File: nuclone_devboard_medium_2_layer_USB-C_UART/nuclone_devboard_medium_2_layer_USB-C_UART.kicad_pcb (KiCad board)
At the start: 2 copper layers, 50 x 76.2 mm, 36 parts, among them J1 JTAG_2X05, J2 TYPE-C-31-M-12, J5 Conn_02x06_Odd_Even, SW1 RESET, SW2 Bootloader, U1 MCP1702-3.3V, U2 TPESD0504C6

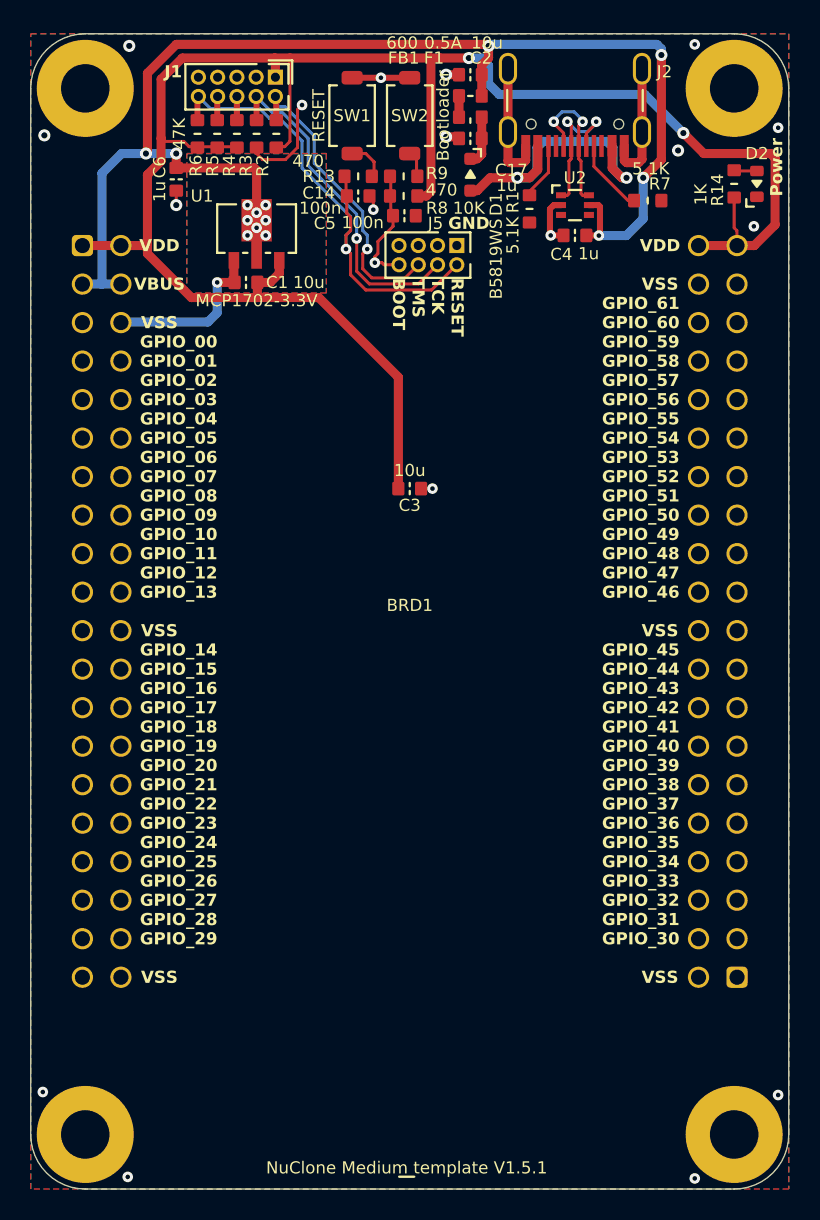
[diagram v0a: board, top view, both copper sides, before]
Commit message: updated medium nuclone footprint in templates, updated library
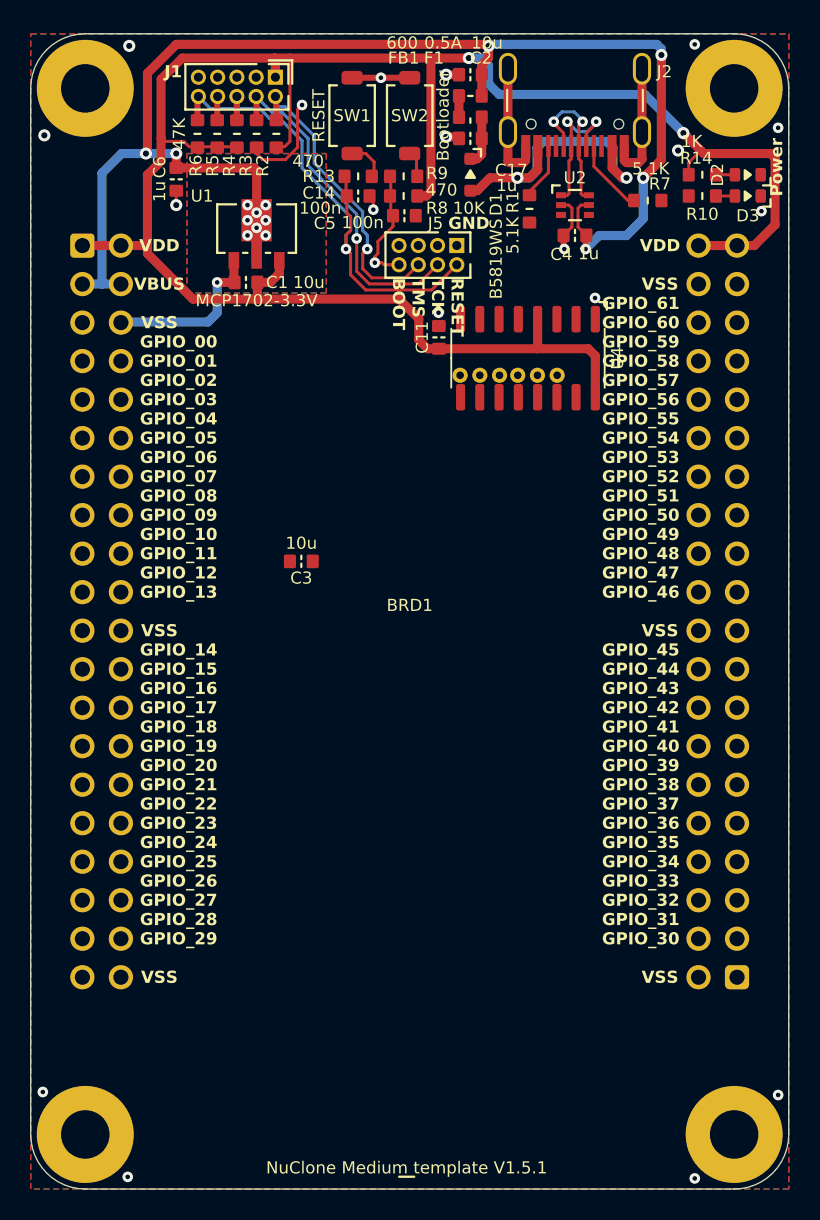
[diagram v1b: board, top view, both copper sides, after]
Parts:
- added C11: 10u, SquantorCapacitor:C_0603, F.Cu at (56.9, 50.0)
- added D3: RED, SquantorDiodes:LED_0603_hand, F.Cu at (77.3, 40.7)
- added R10: 1K, SquantorResistor:R_0603_hand, F.Cu at (74.3, 40.7)
- added TP10: CTS, SquantorTestPoints:TestPoint_hole_H05R10, B.Cu at (58.3, 52.5)
- added TP5: RTS, SquantorTestPoints:TestPoint_hole_H05R10, B.Cu at (64.7, 52.5)
- added TP6: DTR, SquantorTestPoints:TestPoint_hole_H05R10, B.Cu at (63.4, 52.5)
- added TP7: DCD, SquantorTestPoints:TestPoint_hole_H05R10, B.Cu at (62.1, 52.5)
- added TP8: RI, SquantorTestPoints:TestPoint_hole_H05R10, B.Cu at (60.9, 52.5)
- added TP9: DSR, SquantorTestPoints:TestPoint_hole_H05R10, B.Cu at (59.6, 52.5)
- added U4: CH340B, SquantorIC:SOIC-16_3.9x9.9mm_P1.27mm, F.Cu at (62.8, 51.4)
- moved C3 8.61 mm to (47.9, 64.8)
- moved R14 2.18 mm to (74.3, 39.3), turned to 180 degrees
- moved D2 0.85 mm to (77.3, 39.3), turned to 180 degrees
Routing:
- net /VDD: track 127.8 -> 137.1 mm
- net /VBUS: track 89.4 -> 90.8 mm
- net Net-(D3-A): track 0.00 -> 1.25 mm
- net /VSS: track 44.9 -> 45.2 mm, vias 19 -> 20

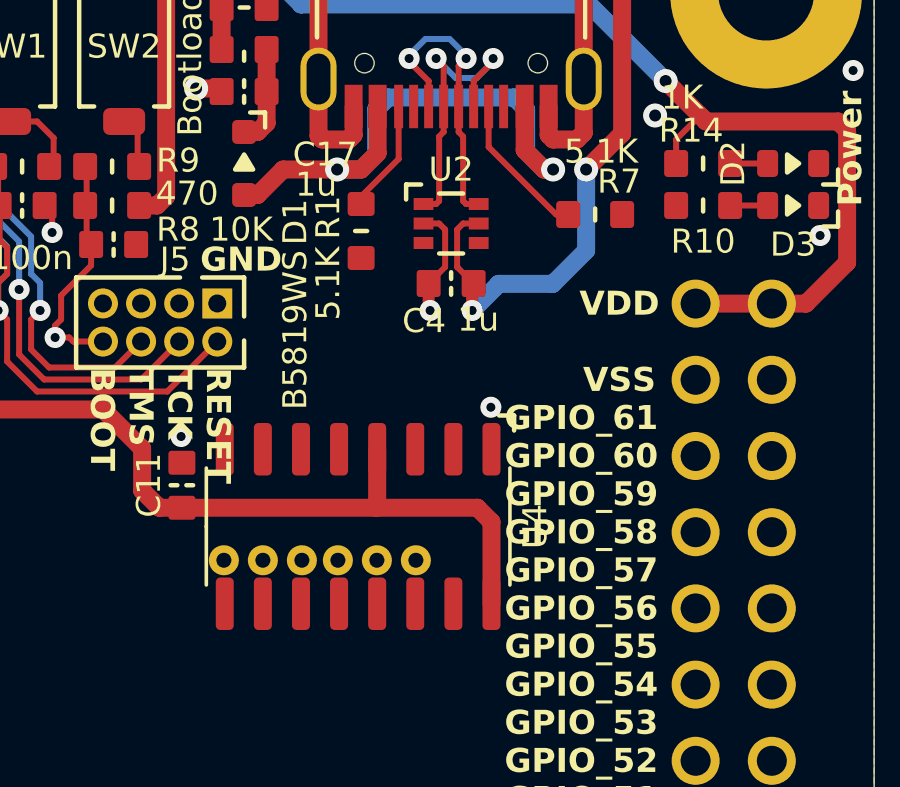
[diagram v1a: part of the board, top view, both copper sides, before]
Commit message: small UART changes
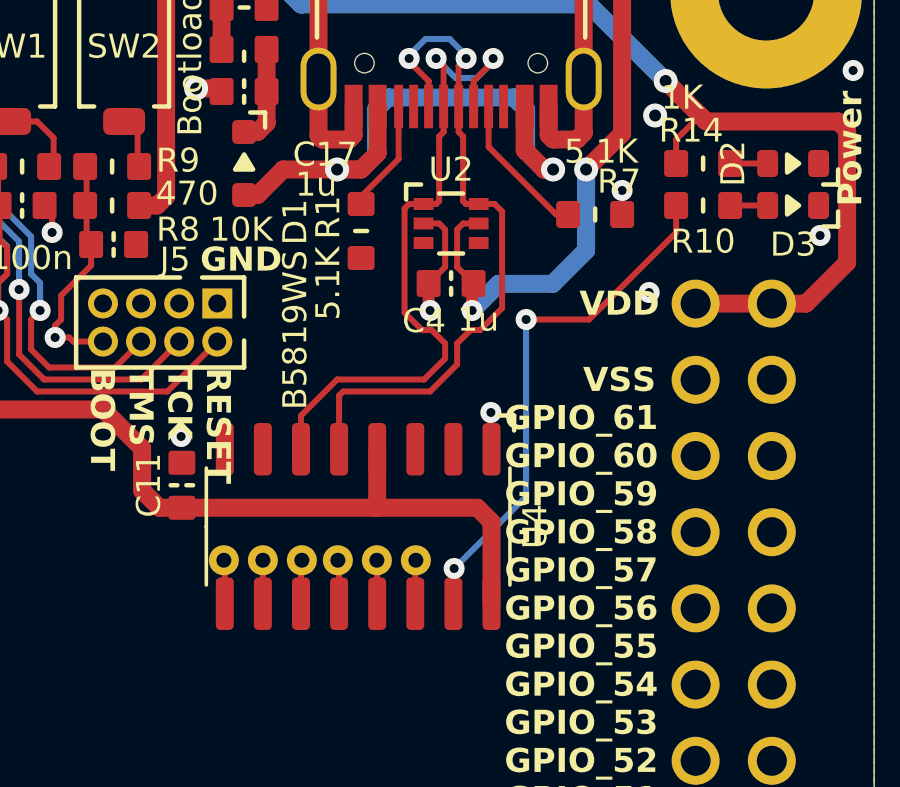
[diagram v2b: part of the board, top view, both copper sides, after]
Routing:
- net /TNOW: track 0.00 -> 17.6 mm, vias 0 -> 2
- net /DN: track 9.84 -> 23.0 mm
- net /DP: track 10.6 -> 23.6 mm
- net Net-(U4-DCD#): track 0.00 -> 1.47 mm
- net Net-(U4-RI#): track 0.00 -> 1.46 mm
- net Net-(U4-CTS#): track 0.00 -> 1.46 mm
- net Net-(U4-RTS#): track 0.00 -> 1.46 mm
- net Net-(U4-DTR#): track 0.00 -> 1.45 mm
- net Net-(U4-DSR#): track 0.00 -> 1.45 mm
- net /VSS: vias 20 -> 22
